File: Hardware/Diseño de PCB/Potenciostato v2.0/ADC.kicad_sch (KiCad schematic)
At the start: 22 parts, among them U3 ADS1255IDBR, X1 XTAL8MHZ

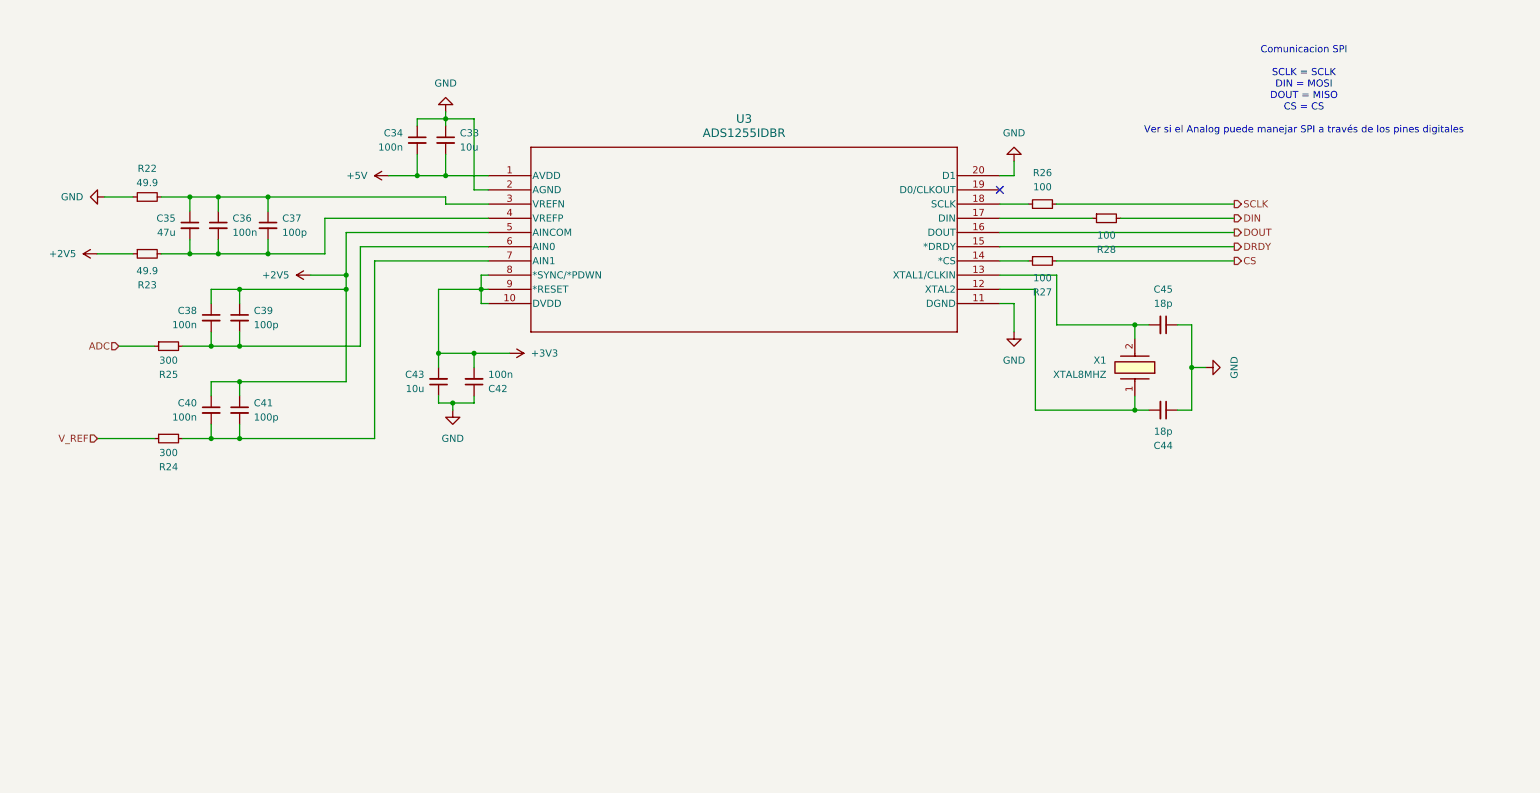
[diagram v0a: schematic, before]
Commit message: Big commit. Hardware was already ready. Board arrived. Hardware testing phase and software development is ongoing, some hardware issues were detected and noted down in the KiCad project for future versions and design corrections. First software libraries under development for ADC, GPIO, Muxes and DAC managment (ADS1255, MAX5217, MAX4737, MAX4617 and GPIO)
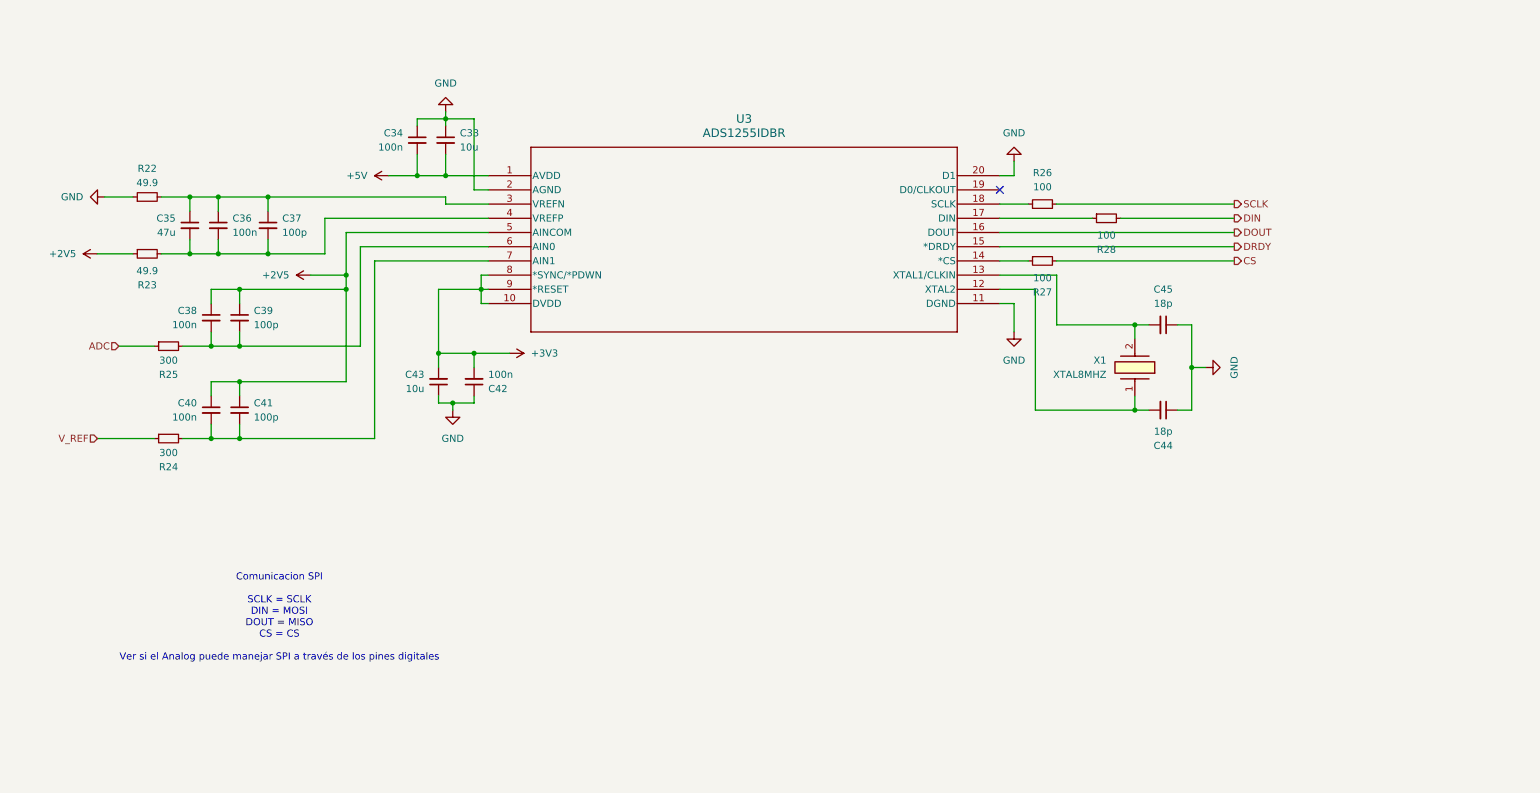
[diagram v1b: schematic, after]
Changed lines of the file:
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@@
 	(text "Comunicacion SPI\n\nSCLK = SCLK\nDIN = MOSI\nDOUT = MISO\nCS = CS\n\nVer si el Analog puede manejar SPI a través de los pines digitales"
 		(exclude_from_sim no)
-		(at 261.366 57.15 0)
+		(at 78.232 151.384 0)
 		(effects
 			(font

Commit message: Hardware modifications. More notes added to the KiCad project related to hardware issues found during testing. USB Power and ground inverted corrected in design and PCB. MAX4477 replaced by OPA2320 in design and PCB. More notes with recommendations and advised can now be found in the schematics.
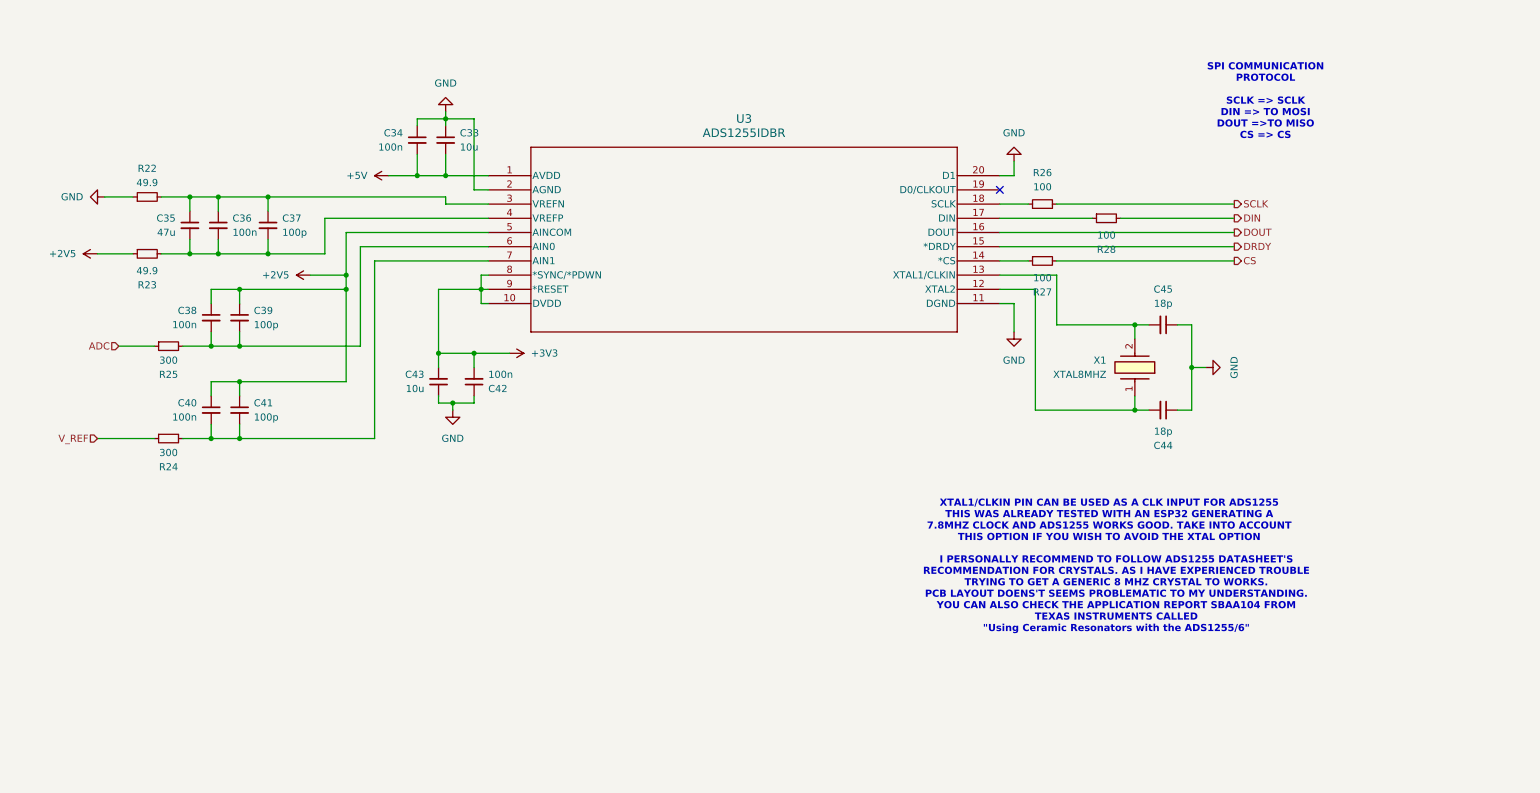
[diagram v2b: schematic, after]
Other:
- note added: "I PERSONALLY RECOMMEND TO FOLLOW ADS1255 DATASHEET'S RECOMMENDATION FOR CRYSTALS. AS I HAVE EXPERIENCED TROUBLE TRYING TO GET A GENERIC 8 MHZ CRYSTAL TO WORKS. PCB LAYOUT DOENS'T SEEMS PROBLEMATIC TO MY UNDERSTANDING. YOU CAN ALSO CHECK THE APPLICATION REPORT SBAA104 FROM TEXAS INSTRUMENTS CALLED "Using Ceramic Resonators with the ADS1255/6""
- note added: "SPI COMMUNICATION PROTOCOL SCLK => SCLK DIN => TO MOSI DOUT =>TO MISO CS => CS"
- note added: "XTAL1/CLKIN PIN CAN BE USED AS A CLK INPUT FOR ADS1255 THIS WAS ALREADY TESTED WITH AN ESP32 GENERATING A 7.8MHZ CLOCK AND ADS1255 WORKS GOOD. TAKE INTO ACCOUNT THIS OPTION IF YOU WISH TO AVOID THE XTAL OPTION"
- note removed: "Comunicacion SPI SCLK = SCLK DIN = MOSI DOUT = MISO CS = CS Ver si el Analog puede manejar SPI a través de los pines digitales"
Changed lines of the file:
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@@
 		)
 	)
-	(text "Comunicacion SPI\n\nSCLK = SCLK\nDIN = MOSI\nDOUT = MISO\nCS = CS\n\nVer si el Analog puede manejar SPI a través de los pines digitales"
+	(text "SPI COMMUNICATION\nPROTOCOL\n\nSCLK => SCLK\nDIN => TO MOSI\nDOUT =>TO MISO\nCS => CS"
 		(exclude_from_sim no)
-		(at 78.232 151.384 0)
+		(at 254.508 59.182 0)
 		(effects
 			(font
 				(size 1.27 1.27)
-				(color 255 0 19 1)
+				(thickness 0.254)
+				(bold yes)
 			)
 		)
+	)
+	(text "XTAL1/CLKIN PIN CAN BE USED AS A CLK INPUT FOR ADS1255\nTHIS WAS ALREADY TESTED WITH AN ESP32 GENERATING A \n7.8MHZ CLOCK AND ADS1255 WORKS GOOD. TAKE INTO ACCOUNT\nTHIS OPTION IF YOU WISH TO AVOID THE XTAL OPTION\n"
+		(exclude_from_sim no)
+		(at 226.568 134.112 0)
+		(effects
+			(font
+				(size 1.27 1.27)
+				(thickness 0.254)
+				(bold yes)
+				(color 255 0 11 1)
+			)
+		)
+	)
+	(text "I PERSONALLY RECOMMEND TO FOLLOW ADS1255 DATASHEET'S \nRECOMMENDATION FOR CRYSTALS. AS I HAVE EXPERIENCED TROUBLE\nTRYING TO GET A GENERIC 8 MHZ CRYSTAL TO WORKS.\nPCB LAYOUT DOENS'T SEEMS PROBLEMATIC TO MY UNDERSTANDING.\nYOU CAN ALSO CHECK THE APPLICATION REPORT SBAA104 FROM\nTEXAS INSTRUMENTS CALLED \n\"Using Ceramic Resonators with the ADS1255/6\""
+		(exclude_from_sim no)
+		(at 227.838 147.32 0)
+		(effects
+			(font
+				(size 1.27 1.27)
+				(thickness 0.254)
+				(bold yes)
+			)
+		)

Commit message: Further documentation and notes on the schematic. Software updates: In MAX4617, corrections in write function, more robust code verification to prevent overflows. In MUX, correction to MAX4617 gain codification and pinout updgraded for MAX4737. ADS1255, mux configured to AIN0-AINCOM in ADS_Initialized.
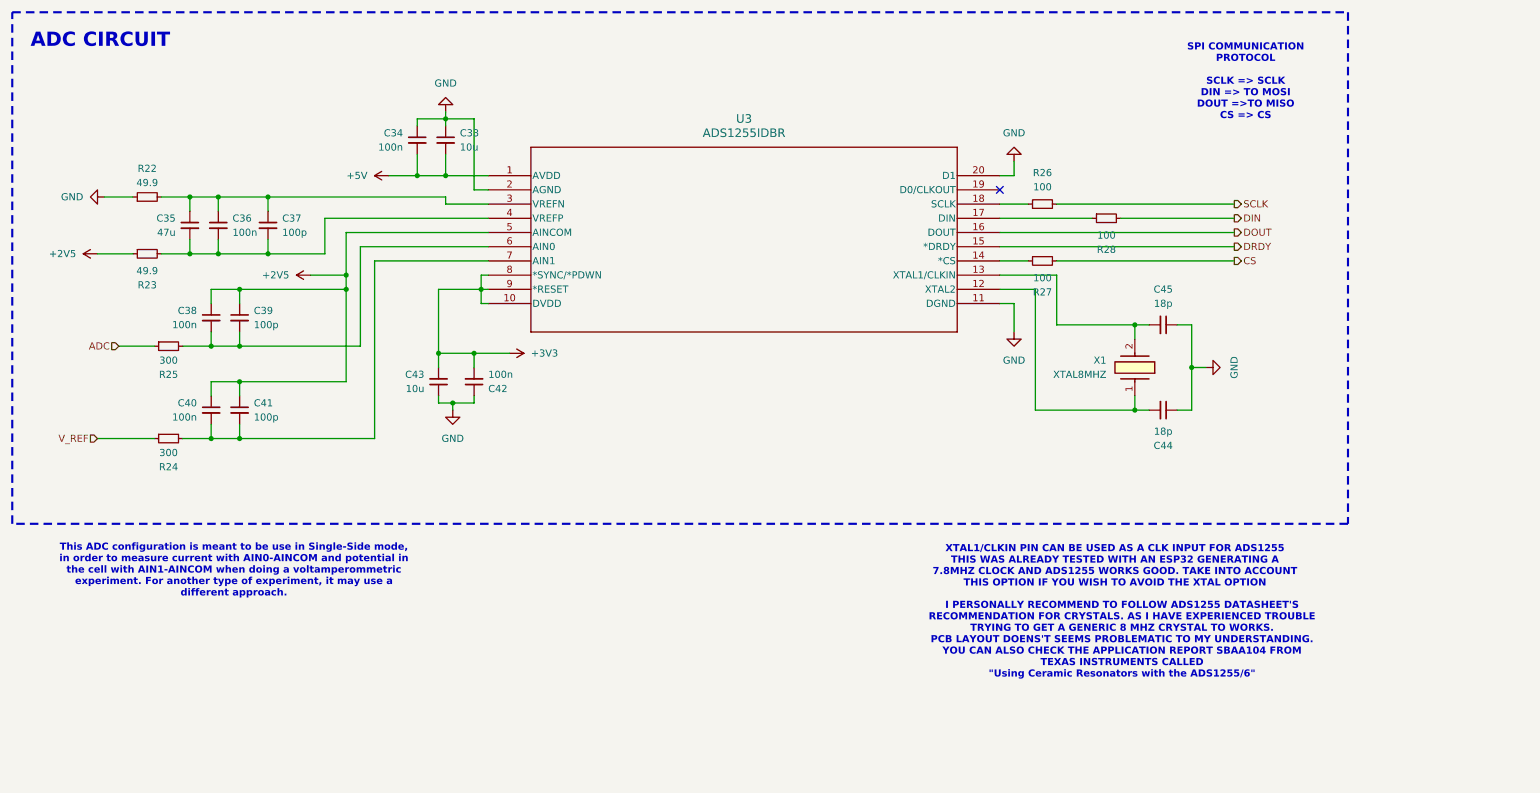
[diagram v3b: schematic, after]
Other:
- note added: "ADC CIRCUIT"
- note added: "This ADC configuration is meant to be use in Single-Side mode, in order to measure current with AIN0-AINCOM and potential in the cell with AIN1-AINCOM when doing a voltamperommetric experiment. For another type of experiment, it may use a different approach."
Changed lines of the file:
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@@
+		)
+	)
+	(rectangle
+		(start 30.48 43.18)
+		(end 269.24 134.62)
+		(stroke
+			(width 0.381)
+			(type dash)
+		)
+		(fill
+			(type none)
 		)
 	)
 	(text "SPI COMMUNICATION\nPROTOCOL\n\nSCLK => SCLK\nDIN => TO MOSI\nDOUT =>TO MISO\nCS => CS"
 		(exclude_from_sim no)
-		(at 254.508 59.182 0)
+		(at 250.952 55.626 0)
 		(effects
 			(font
@@
 		)
 	)
+	(text "This ADC configuration is meant to be use in Single-Side mode,\nin order to measure current with AIN0-AINCOM and potential in\nthe cell with AIN1-AINCOM when doing a voltamperommetric\nexperiment. For another type of experiment, it may use a \ndifferent approach."
+		(exclude_from_sim no)
+		(at 70.104 143.002 0)
+		(effects
+			(font
+				(face "KiCad Font")
+				(size 1.27 1.27)
+				(thickness 0.254)
+				(bold yes)
+			)
+		)
+	)
 	(text "XTAL1/CLKIN PIN CAN BE USED AS A CLK INPUT FOR ADS1255\nTHIS WAS ALREADY TESTED WITH AN ESP32 GENERATING A \n7.8MHZ CLOCK AND ADS1255 WORKS GOOD. TAKE INTO ACCOUNT\nTHIS OPTION IF YOU WISH TO AVOID THE XTAL OPTION\n"
 		(exclude_from_sim no)
-		(at 226.568 134.112 0)
+		(at 227.584 142.24 0)
 		(effects
 			(font
@@
 	(text "I PERSONALLY RECOMMEND TO FOLLOW ADS1255 DATASHEET'S \nRECOMMENDATION FOR CRYSTALS. AS I HAVE EXPERIENCED TROUBLE\nTRYING TO GET A GENERIC 8 MHZ CRYSTAL TO WORKS.\nPCB LAYOUT DOENS'T SEEMS PROBLEMATIC TO MY UNDERSTANDING.\nYOU CAN ALSO CHECK THE APPLICATION REPORT SBAA104 FROM\nTEXAS INSTRUMENTS CALLED \n\"Using Ceramic Resonators with the ADS1255/6\""
 		(exclude_from_sim no)
-		(at 227.838 147.32 0)
+		(at 228.854 155.448 0)
 		(effects
 			(font
@@
 				(bold yes)
 			)
+		)
+	)
+	(text "ADC CIRCUIT\n"
+		(exclude_from_sim no)
+		(at 46.228 48.26 0)
+		(effects
+			(font
+				(size 2.54 2.54)
+				(thickness 0.508)
+				(bold yes)
+			)

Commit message: Hardware: Hardware Corrections in Potentiostat, small but important ones (WE electrode, Normal Open connection for electric disconnection in schematic and PCB. DAC I2C pull up resistors connected to 5V PCB layout corrected.). New project for ESP32 board: board design to hold ESP32 and LevelShifter for I2C3.3V to 5V. No more. No big changes in firmware and software, nothing to note, really small corrections in that were in the way.
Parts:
- added U12: ~, symbol Graphics_images:UNS_logo
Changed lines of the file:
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@@
+	)
+	(symbol
+		(lib_id "Graphics_images:UNS_logo")
+		(at 238.76 166.37 0)
+		(unit 1)
+		(exclude_from_sim no)
+		(in_bom no)
+		(on_board no)
+		(dnp yes)
+		(fields_autoplaced yes)
+		(property "Reference" "U12"
+			(at 237.998 161.798 0)
+			(effects
+				(font
+					(size 1.27 1.27)
+				)
+				(justify left)
+				(hide yes)
+			)
+		)
+		(property "Value" "~"
+			(at 218.44 157.48 0)
+			(effects
+				(font
+					(size 1.27 1.27)
+				)
+				(justify left)
+			)
+		)
+		(property "Footprint" ""
+			(at 229.87 162.56 0)
+			(effects
+				(font
+					(size 1.27 1.27)
+				)
+				(hide yes)
+			)
+		)
+		(property "Datasheet" ""
+			(at 229.87 162.56 0)
+			(effects
+				(font
+					(size 1.27 1.27)
+				)
+				(hide yes)
+			)
+		)
+		(property "Description" ""
+			(at 229.87 162.56 0)
+			(effects
+				(font
+					(size 1.27 1.27)
+				)
+				(hide yes)
+			)
+		)
+		(property "JLCLIB" ""
+			(at 238.76 166.37 0)
+			(effects
+				(font
+					(size 1.27 1.27)
+				)
+				(hide yes)
+			)
+		)
+		(instances
+			(project "Potenciostato v2.0"
+				(path "/3273751a-bb69-4014-b380-866ff743e010/5e65dc78-f111-4dc8-9e0e-9fe2045a751d"
+					(reference "U12")
+					(unit 1)
+				)
+			)
+		)
 	)
 	(symbol
